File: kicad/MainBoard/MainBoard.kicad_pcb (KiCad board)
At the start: 2 copper layers, 191.5 x 166.3 mm, 105 parts, among them J1 CHAN1, J10 ACC Port, J11 433TX, J12 VDC INPUT, J13 BAT, J14 TRG1, J15 TRG2, J16 FP-BUTTONS, J17 EXPAN2, J18 OUTPUT_BOARD_POWER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

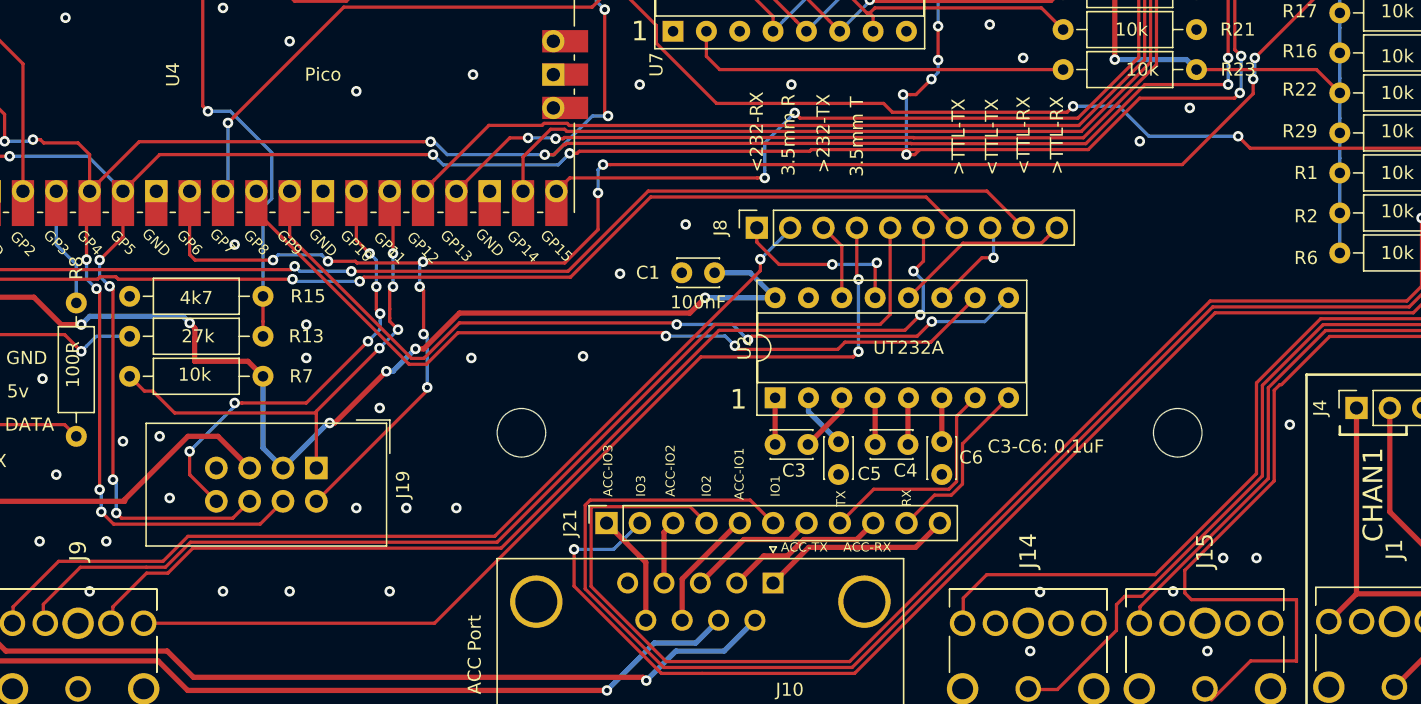
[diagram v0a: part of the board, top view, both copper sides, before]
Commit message: No more 12v rs232 - move to UART
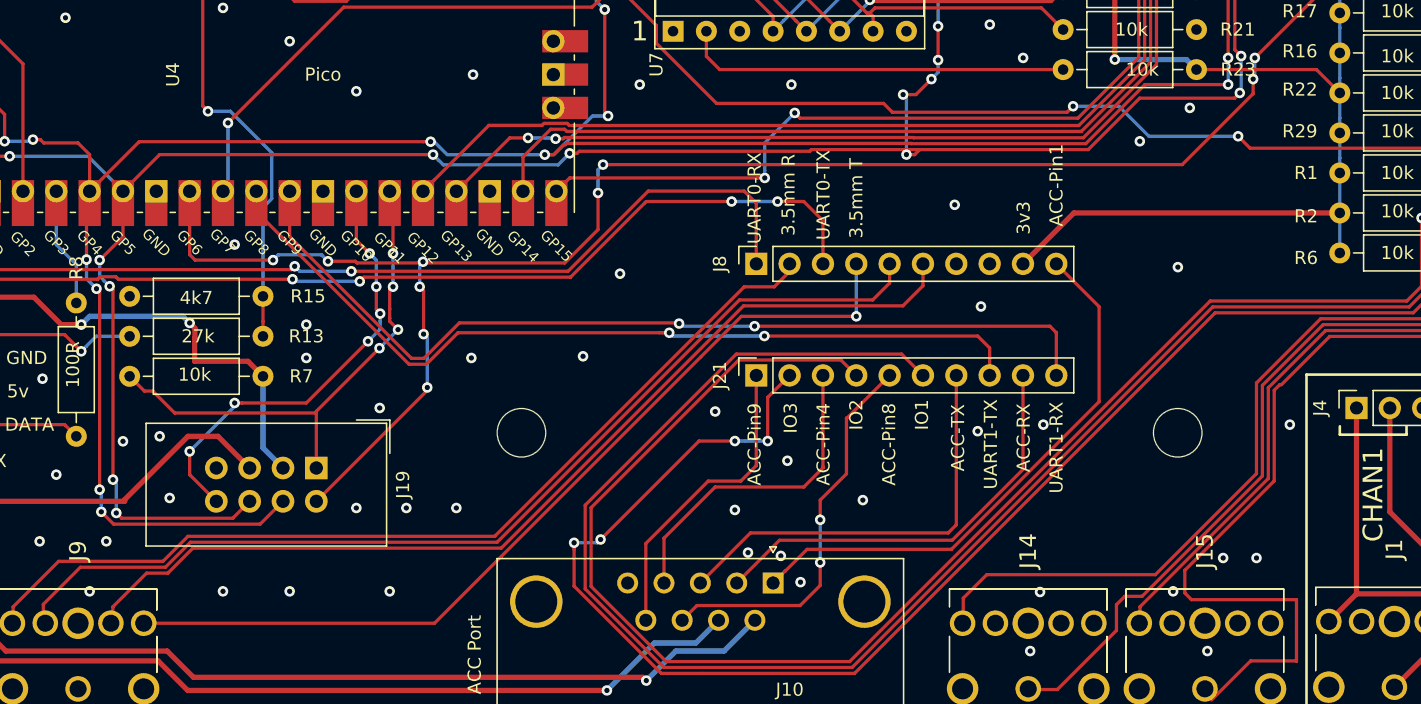
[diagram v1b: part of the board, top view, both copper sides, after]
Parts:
- removed C1: 100nF, Capacitor_THT:C_Disc_D3.0mm_W2.0mm_P2.50mm
- removed C3, C4, C5, C6: 0.1uF, Capacitor_THT:C_Disc_D3.0mm_W2.0mm_P2.50mm
- removed U2: UT232A, Package_DIP:DIP-16_W7.62mm_Socket
- J21: footprint Connector_PinSocket_2.54mm:PinSocket_1x11_P2.54mm_Vertical -> Connector_PinSocket_2.54mm:PinSocket_1x10_P2.54mm_Vertical
- J9: value AudioJack3_SwitchTR -> Aux
- moved J21 16.0 mm to (104.1, 155.0)
- moved J8 2.75 mm to (104.1, 146.5)
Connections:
- J21 pad 10: 232-RX -> MCU-UART1-RX
- J21 pad 8: 232-TX -> MCU-UART1-TX
- J8 pad 1: 3.5-232-RX -> MCU-UART0-RX
- J8 pad 10: TTL-SER-0-RX -> ACCP-PIN1
- J8 pad 3: 3.5-232-TX -> MCU-UART0-TX
- J8 pad 7: MCU-UART0-TX -> unconnected-(J8-Pin_7-Pad7)
- J8 pad 8: TTL-SER-0-TX -> unconnected-(J8-Pin_8-Pad8)
- J8 pad 9: MCU-UART0-RX -> 3v3
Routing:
- net ACCP-PIN1: track 14.6 -> 42.4 mm
- net ACCP-232-TX: track 9.98 -> 32.7 mm
- net 3v3: track 530.9 -> 508.4 mm, vias 26 -> 22
- net ACCP-IO-3: track 9.31 -> 29.8 mm, vias 0 -> 2
- net ACCP-232-RX: track 12.8 -> 33.1 mm
- net ACCP-IO-2: track 4.85 -> 24.8 mm
- net Net-(J21-Pin_2): track 96.0 -> 114.3 mm, vias 1 -> 4
- net 232-TX: track 17.2 -> 0.00 mm
- net MCU-UART0-RX: track 90.7 -> 74.2 mm
- net Net-(J21-Pin_4): track 104.9 -> 120.9 mm
- net Net-(J21-Pin_6): track 113.2 -> 129.2 mm
- net ACCP-IO-1: track 8.65 -> 23.6 mm
- net 3.5-232-RX: track 13.7 -> 0.00 mm, vias 2 -> 0
- net 232-RX: track 13.5 -> 0.00 mm
- net TTL-SER-0-RX: track 13.5 -> 0.00 mm
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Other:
- board text added: "ACC-Pin1"
- board text added: "ACC-Pin4"
- board text added: "ACC-Pin8"
- board text added: "ACC-Pin9"
- board text added: "UART0-RX"
- board text added: "UART0-TX"
- board text added: "UART1-RX"
- board text added: "UART1-TX"
- board text removed: "<232-RX"
- board text removed: "<TTL-RX"
- board text removed: "<TTL-TX"
- board text removed: ">232-TX"
- board text removed: ">TTL-RX"
- board text removed: ">TTL-TX"
- board text removed: "ACC-IO1"
- board text removed: "ACC-IO2"
- board text removed: "ACC-IO3"
- board text removed: "C3-C6: 0.1uF"
- board text removed: "RX"
- board text removed: "TX"

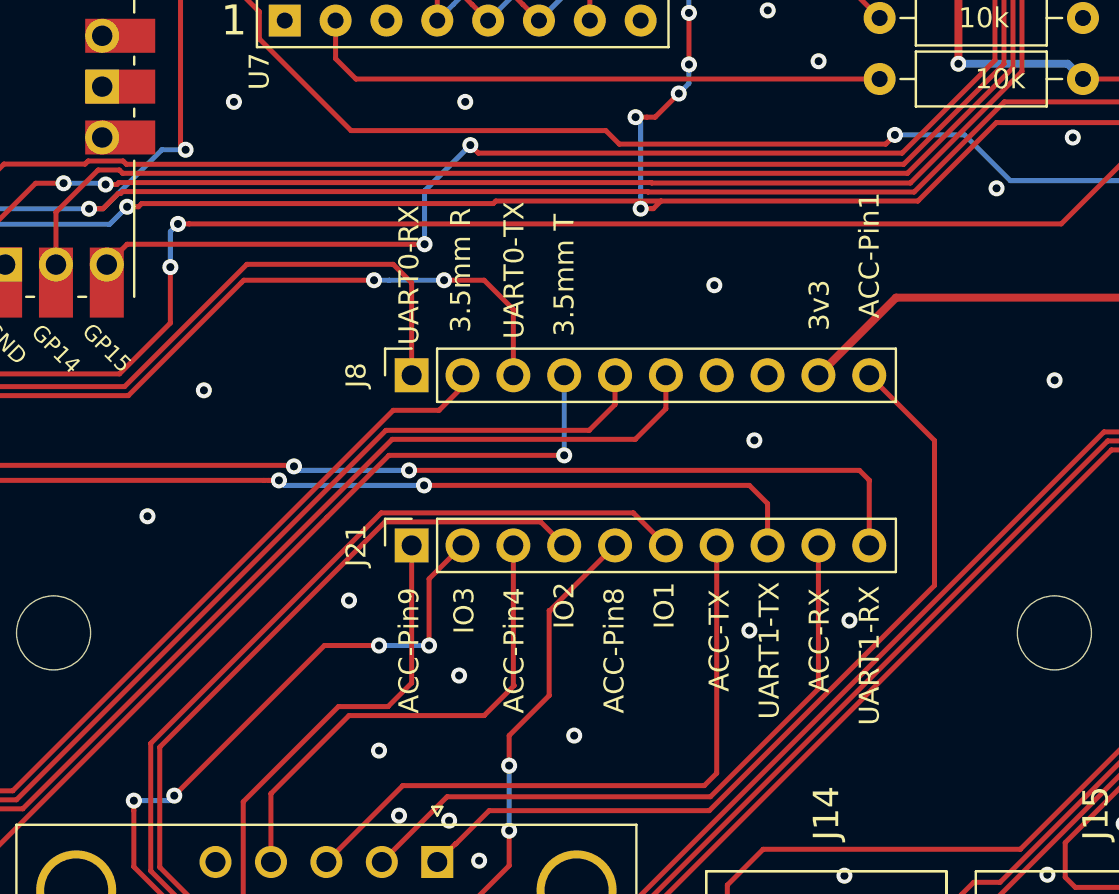
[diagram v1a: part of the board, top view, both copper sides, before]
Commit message: Small changes to expander
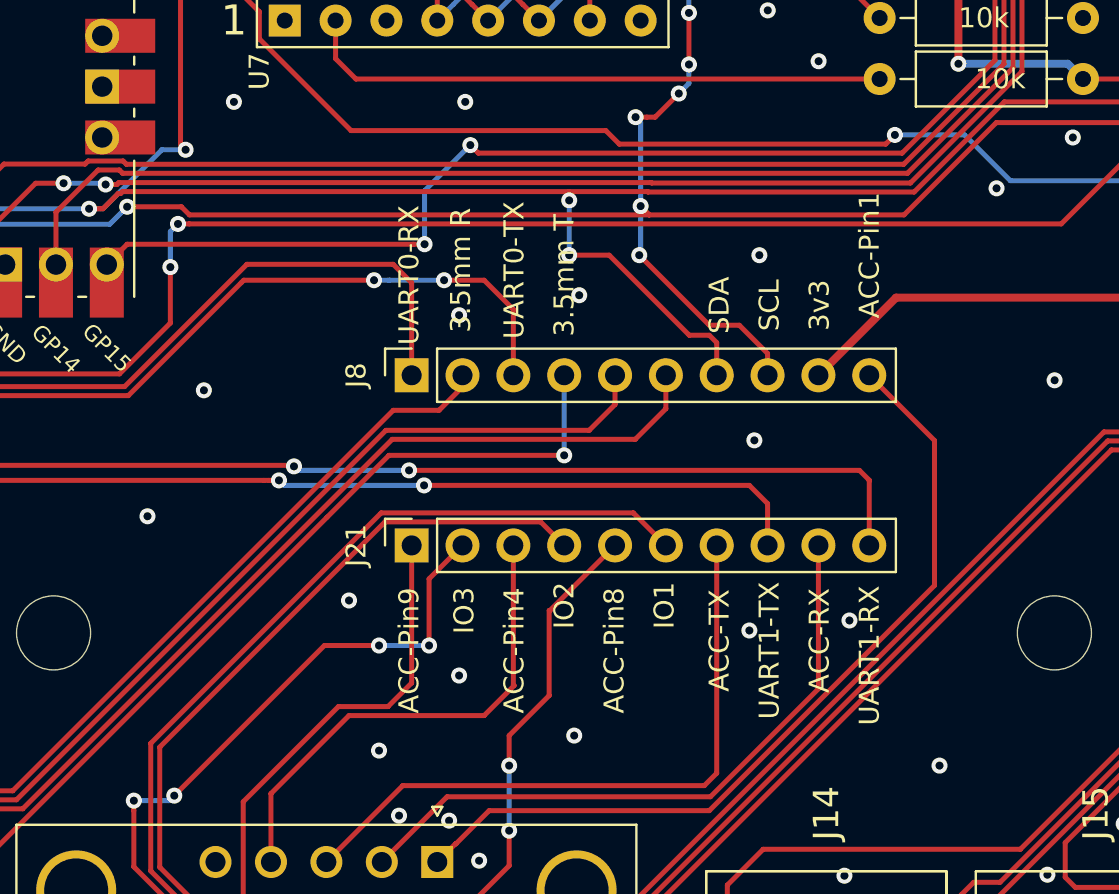
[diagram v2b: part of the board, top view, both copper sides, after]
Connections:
- J8 pad 7: unconnected-(J8-Pin_7-Pad7) -> SDA
- J8 pad 8: unconnected-(J8-Pin_8-Pad8) -> SCL
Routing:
- net SDA: track 414.5 -> 428.5 mm, vias 19 -> 21
- net SCL: track 402.9 -> 414.6 mm, vias 18 -> 19
- net GND: vias 119 -> 122

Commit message: More tiny mainboard updates
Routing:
- net SDA: track 428.5 -> 426.5 mm
- net SCL: track 414.6 -> 416.2 mm
- net 3v3: track 508.4 -> 509.2 mm
- net GND: vias 122 -> 125

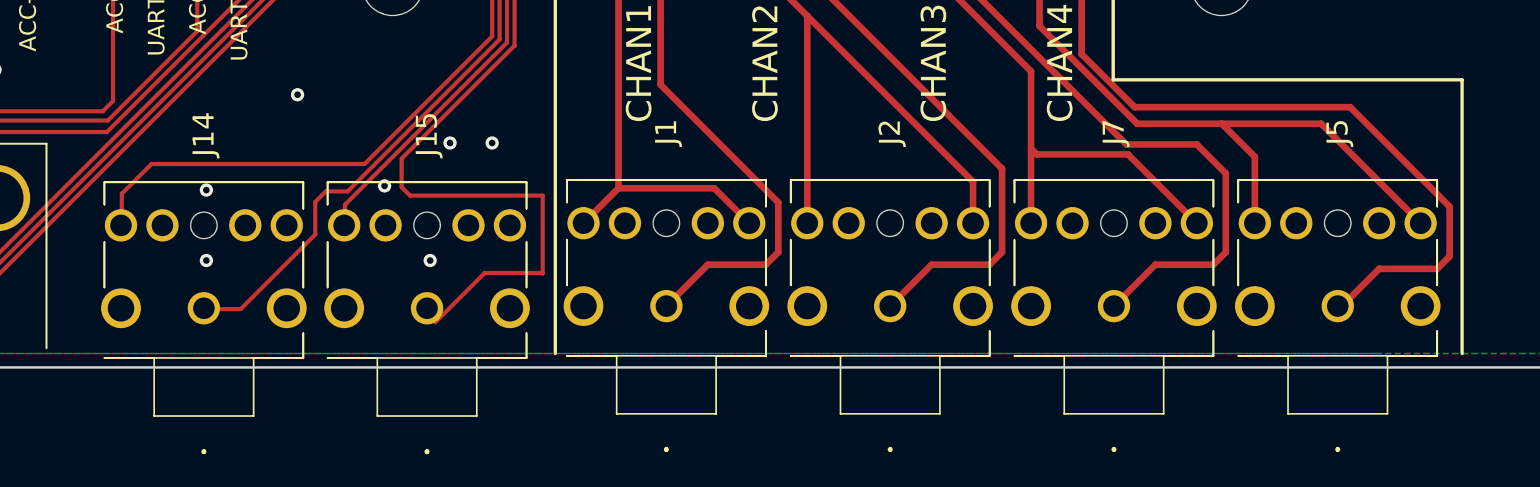
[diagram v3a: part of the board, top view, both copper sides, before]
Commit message: FrontPanel MainBoard alignment
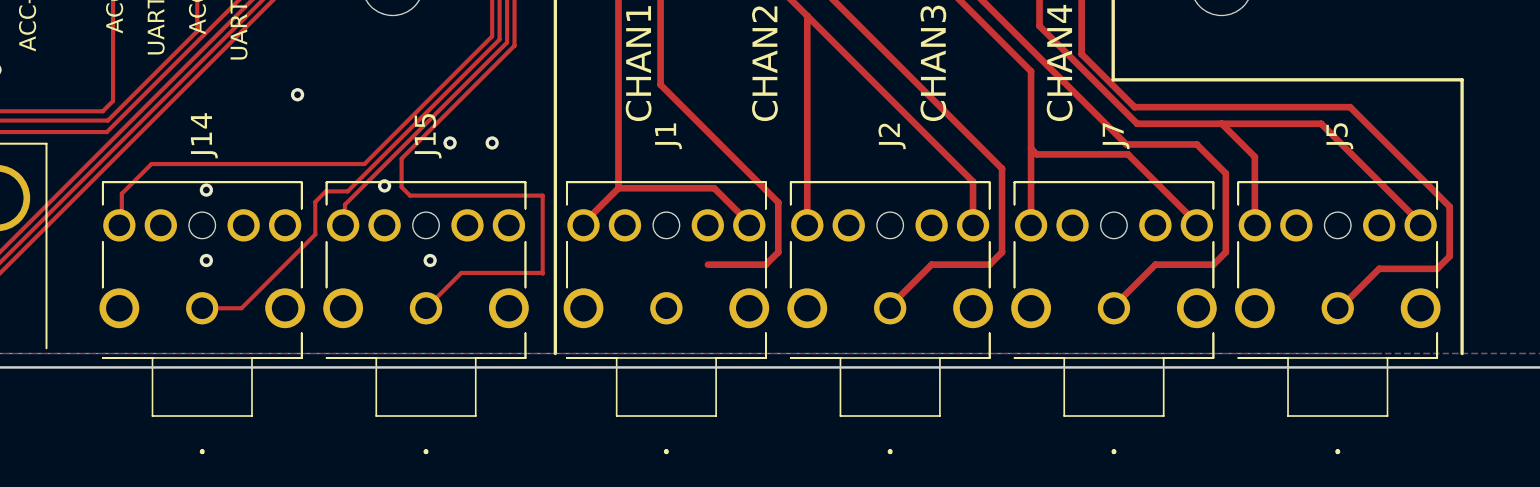
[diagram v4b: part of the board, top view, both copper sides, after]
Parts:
- moved J1 0.13 mm to (152.8, 178.9)
- moved J2 0.13 mm to (166.2, 178.9)
- moved J5 0.13 mm to (193.2, 178.9)
- moved J7 0.13 mm to (179.8, 178.9)
- moved J14 0.10 mm to (124.8, 178.9)
- moved J15 0.06 mm to (138.2, 178.9)
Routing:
- net Net-(J4-Pin_2): track 29.1 -> 25.5 mm
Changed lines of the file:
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@@
 		(solder_mask_min_width 0.25)
 		(allow_soldermask_bridges_in_footprints no)
+		(grid_origin 15.500364 182.450548)
 		(pcbplotparams
 			(layerselection 0x00010fc_ffffffff)
@@
 		(model "${KIPRJMOD}/3d/DC-005-2.5A-2.0.stp"
 			(offset
-				(xyz 12 -6.75 6)
+				(xyz 11.8 -6.9 5.53)
 			)
 			(scale
@@
 	(footprint "ProjLib:STX31005N"
 		(layer "F.Cu")
-		(at 124.85 178.88 90)
+		(at 124.750364 178.88 90)
 		(descr "STX-3100-5N-1")
 		(tags "Connector")
@@
 		(model "${KIPRJMOD}/3d/STX-3100-3N.stp"
 			(offset
-				(xyz -2.5 0 5)
+				(xyz -2.5 0 4.97)
 			)
 			(scale
@@
 		(model "${KIPRJMOD}/3d/STX-3100-3N.stp"
 			(offset
-				(xyz -2.5 0 5)
+				(xyz -2.5 0 4.97)
 			)
 			(scale
@@
 	(footprint "ProjLib:STX31005N"
 		(layer "F.Cu")
-		(at 152.75 178.75 90)
+		(at 152.75 178.88 90)
 		(descr "STX-3100-5N-1")
 		(tags "Connector")
@@
 		(model "${KIPRJMOD}/3d/STX-3100-3N.stp"
 			(offset
-				(xyz -2.5 0 5)
+				(xyz -2.5 0 4.97)
 			)
 			(scale
@@
 	(footprint "ProjLib:STX31005N"
 		(layer "F.Cu")
-		(at 138.312 178.88 90)
+		(at 138.25 178.88 90)
 		(descr "STX-3100-5N-1")
 		(tags "Connector")
@@
 		(model "${KIPRJMOD}/3d/STX-3100-3N.stp"
 			(offset
-				(xyz -2.5 0 5)
+				(xyz -2.5 0 4.97)
 			)
 			(scale
@@
 	(footprint "ProjLib:STX31005N"
 		(layer "F.Cu")
-		(at 166.25 178.75 90)
+		(at 166.25 178.88 90)
 		(descr "STX-3100-5N-1")
 		(tags "Connector")
@@
 		(model "${KIPRJMOD}/3d/STX-3100-3N.stp"
 			(offset
-				(xyz -2.5 0 5)
+				(xyz -2.5 0 4.97)
 			)
 			(scale
@@
 	(footprint "ProjLib:STX31005N"
 		(layer "F.Cu")
-		(at 193.25 178.75 90)
+		(at 193.25 178.88 90)
 		(descr "STX-3100-5N-1")
 		(tags "Connector")
@@
 		(model "${KIPRJMOD}/3d/STX-3100-3N.stp"
 			(offset
-				(xyz -2.5 0 5)
+				(xyz -2.5 0 4.97)
 			)
 			(scale
@@
 	(footprint "ProjLib:STX31005N"
 		(layer "F.Cu")
-		(at 179.75 178.75 90)
+		(at 179.75 178.88 90)
 		(descr "STX-3100-5N-1")
 		(tags "Connector")
@@
 		(model "${KIPRJMOD}/3d/STX-3100-3N.stp"
 			(offset
-				(xyz -2.5 0 5)
+				(xyz -2.5 0 4.97)
 			)
 			(scale
@@
 	)
 	(segment
-		(start 152.75 178.75)
-		(end 155.25 176.25)
-		(width 0.4)
-		(layer "F.Cu")
-		(net 13)
-	)
-	(segment
 		(start 155.64 171.64)
 		(end 157.75 173.75)
@@
 	)
 	(segment
-		(start 158.75 136.525)
-		(end 159.88137 136.525)
+		(start 132.207 171.831)
+		(end 133.52459 171.831)
 		(width 0.25)
 		(layer "F.Cu")
@@
 	)
 	(segment
-		(start 131.572 174.428)
-		(end 131.572 172.466)
+		(start 131.572 172.466)
+		(end 132.207 171.831)
 		(width 0.25)
 		(layer "F.Cu")
@@
 	)
 	(segment
-		(start 142.690011 162.665579)
-		(end 142.690011 155.758578)
+		(start 158.75 136.525)
+		(end 159.88137 136.525)
 		(width 0.25)
 		(layer "F.Cu")
@@
 	)
 	(segment
-		(start 133.52459 171.831)
-		(end 142.690011 162.665579)
+		(start 158.620184 151.129997)
+		(end 164.084 145.66618)
 		(width 0.25)
 		(layer "F.Cu")
@@
 	)
 	(segment
-		(start 132.207 171.831)
-		(end 133.52459 171.831)
+		(start 147.318592 151.129997)
+		(end 158.620184 151.129997)
 		(width 0.25)
 		(layer "F.Cu")
@@
 	)
 	(segment
-		(start 131.572 172.466)
-		(end 132.207 171.831)
+		(start 127.12 178.88)
+		(end 131.572 174.428)
 		(width 0.25)
 		(layer "F.Cu")
@@
 	)
 	(segment
-		(start 124.85 178.93)
-		(end 127.07 178.93)
+		(start 142.690011 155.758578)
+		(end 147.318592 151.129997)
 		(width 0.25)
 		(layer "F.Cu")
@@
 	)
 	(segment
-		(start 142.690011 155.758578)
-		(end 147.318592 151.129997)
+		(start 124.750364 178.88)
+		(end 127.12 178.88)
 		(width 0.25)
 		(layer "F.Cu")
@@
 	)
 	(segment
-		(start 158.620184 151.129997)
-		(end 164.084 145.66618)
+		(start 164.084 145.66618)
+		(end 164.084 136.271)
 		(width 0.25)
 		(layer "F.Cu")
@@
 	)
 	(segment
-		(start 127.07 178.93)
-		(end 131.572 174.428)
+		(start 131.572 174.428)
+		(end 131.572 172.466)
 		(width 0.25)
 		(layer "F.Cu")
@@
 	)
 	(segment
-		(start 147.318592 151.129997)
-		(end 158.620184 151.129997)
+		(start 133.52459 171.831)
+		(end 142.690011 162.665579)
 		(width 0.25)
 		(layer "F.Cu")
@@
 	)
 	(segment
-		(start 164.084 145.66618)
-		(end 164.084 136.271)
+		(start 142.690011 162.665579)
+		(end 142.690011 155.758578)
 		(width 0.25)
 		(layer "F.Cu")
@@
 	)
 	(segment
-		(start 136.779 169.84941)
-		(end 136.779 171.577)
+		(start 143.590032 156.131378)
+		(end 143.590031 163.038379)
 		(width 0.25)
 		(layer "F.Cu")
@@
 	)
 	(segment
-		(start 143.590032 156.131378)
-		(end 143.590031 163.038379)
+		(start 140.38 176.75)
+		(end 138.25 178.88)
 		(width 0.25)
 		(layer "F.Cu")
@@
 	)
 	(segment
-		(start 147.816981 152.030019)
-		(end 144.145 155.702)
+		(start 165.608 145.415001)
+		(end 158.992984 152.030019)
 		(width 0.25)
 		(layer "F.Cu")
@@
 	)
 	(segment
-		(start 144.01941 155.702)
-		(end 143.590032 156.131378)
+		(start 144.145 155.702)
+		(end 144.01941 155.702)
 		(width 0.25)
 		(layer "F.Cu")
@@
 	)
 	(segment
-		(start 158.992984 152.030019)
-		(end 147.816981 152.030019)
+		(start 136.779 169.84941)
+		(end 136.779 171.577)
 		(width 0.25)
 		(layer "F.Cu")
@@
 	)
 	(segment
-		(start 165.608 145.415001)
-		(end 158.992984 152.030019)
+		(start 145.288 176.784)
+		(end 145.254 176.75)
 		(width 0.25)
 		(layer "F.Cu")
@@
 	)
 	(segment
-		(start 143.590031 163.038379)
-		(end 136.779 169.84941)
+		(start 145.288 172.085)
+		(end 145.288 176.784)
 		(width 0.25)
 		(layer "F.Cu")
@@
 	)
 	(segment
-		(start 145.254 176.75)
-		(end 141.792 176.75)
+		(start 136.779 171.577)
+		(end 137.287 172.085)
 		(width 0.25)
 		(layer "F.Cu")
@@
 	)
 	(segment
-		(start 144.145 155.702)
-		(end 144.01941 155.702)
+		(start 145.254 176.75)
+		(end 140.38 176.75)
 		(width 0.25)
 		(layer "F.Cu")
@@
 	)
 	(segment
-		(start 136.779 171.577)
-		(end 137.287 172.085)
+		(start 137.287 172.085)
+		(end 145.288 172.085)
 		(width 0.25)
 		(layer "F.Cu")
@@
 	)
 	(segment
-		(start 145.288 172.085)
-		(end 145.288 176.784)
+		(start 144.01941 155.702)
+		(end 143.590032 156.131378)
 		(width 0.25)
 		(layer "F.Cu")
@@
 	)
 	(segment
-		(start 137.287 172.085)
-		(end 145.288 172.085)
+		(start 158.992984 152.030019)
+		(end 147.816981 152.030019)
 		(width 0.25)
 		(layer "F.Cu")
@@
 	)
 	(segment
-		(start 165.608 131.191)
-		(end 165.608 145.415001)
+		(start 143.590031 163.038379)
+		(end 136.779 169.84941)
 		(width 0.25)
 		(layer "F.Cu")
@@
 	)
 	(segment
-		(start 145.288 176.784)
-		(end 145.254 176.75)
+		(start 147.816981 152.030019)
+		(end 144.145 155.702)
 		(width 0.25)
 		(layer "F.Cu")
@@
 	)
 	(segment
-		(start 141.792 176.75)
-		(end 138.811 179.731)
+		(start 165.608 131.191)
+		(end 165.608 145.415001)
 		(width 0.25)
 		(layer "F.Cu")
